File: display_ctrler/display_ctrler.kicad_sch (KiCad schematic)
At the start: 48 parts, among them J101 CONN_01x02, J301 USB_C_Receptacle_USB2.0, J302 Micro_SD_Card, U301 USBLC6-2SC6, U302 W25Q128JVS, U303 RP2040, U304 74AHC04, U305 ESP01s, Y301 12MHz

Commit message: finish schm
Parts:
- C301, C302, C304, C305, C306, C307, C308, C309, C310, C311, C312, C313, C314, C315, C316, C318: footprint Capacitor_SMD:C_0402_1005Metric -> Capacitor_SMD:C_0603_1608Metric
- J301: footprint my_footprints:USB_C_7082A -> project_lib:CUI_UJ20-C-V-C-1-SMT-TR
- R301, R302, R303, R304, R305, R306, R307, R308, R309, R311, R312, R313: footprint Resistor_SMD:R_0402_1005Metric -> Resistor_SMD:R_0603_1608Metric
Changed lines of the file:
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@@
 			)
 		)
-		(property "Footprint" "my_footprints:USB_C_7082A"
+		(property "Footprint" "project_lib:CUI_UJ20-C-V-C-1-SMT-TR"
 			(at 33.02 53.34 0)
 			(effects
@@
 			)
 		)
-		(property "Datasheet" "https://www.usb.org/sites/default/files/documents/usb_type-c.zip"
+		(property "Datasheet" "https://www.sameskydevices.com/product/resource/uj20-c-v-c-1-smt-tr.pdf"
 			(at 33.02 53.34 0)
 			(effects
@@
 			)
 		)
-		(property "Footprint" "Resistor_SMD:R_0402_1005Metric"
+		(property "Footprint" "Resistor_SMD:R_0603_1608Metric"
 			(at 276.098 72.39 90)
 			(effects
@@
 			)
 		)
-		(property "Footprint" "Resistor_SMD:R_0402_1005Metric"
+		(property "Footprint" "Resistor_SMD:R_0603_1608Metric"
 			(at 57.15 104.648 90)
 			(effects
@@
 			)
 		)
-		(property "Footprint" "Resistor_SMD:R_0402_1005Metric"
+		(property "Footprint" "Resistor_SMD:R_0603_1608Metric"
 			(at 265.938 72.39 90)
 			(effects
@@
 			)
 		)
-		(property "Footprint" "Resistor_SMD:R_0402_1005Metric"
+		(property "Footprint" "Resistor_SMD:R_0603_1608Metric"
 			(at 41.91 104.648 90)
 			(effects
@@
 			)
 		)
-		(property "Footprint" "Resistor_SMD:R_0402_1005Metric"
+		(property "Footprint" "Resistor_SMD:R_0603_1608Metric"
 			(at 235.458 71.12 90)
 			(effects
@@
 			)
 		)
-		(property "Footprint" "Resistor_SMD:R_0402_1005Metric"
+		(property "Footprint" "Resistor_SMD:R_0603_1608Metric"
 			(at 48.26 47.498 90)
 			(effects
@@
 			)
 		)
-		(property "Footprint" "Capacitor_SMD:C_0402_1005Metric"
+		(property "Footprint" "Capacitor_SMD:C_0603_1608Metric"
 			(at 120.3452 134.62 0)
 			(effects
@@
 			)
 		)
-		(property "Footprint" "Resistor_SMD:R_0402_1005Metric"
+		(property "Footprint" "Resistor_SMD:R_0603_1608Metric"
 			(at 131.318 64.77 90)
 			(effects
@@
 			)
 		)
-		(property "Footprint" "Capacitor_SMD:C_0402_1005Metric"
+		(property "Footprint" "Capacitor_SMD:C_0603_1608Metric"
 			(at 230.1748 36.83 0)
 			(effects
@@
 			)
 		)
-		(property "Footprint" "Capacitor_SMD:C_0402_1005Metric"
+		(property "Footprint" "Capacitor_SMD:C_0603_1608Metric"
 			(at 218.7448 36.83 0)
 			(effects
@@
 			)
 		)
-		(property "Footprint" "Resistor_SMD:R_0402_1005Metric"
+		(property "Footprint" "Resistor_SMD:R_0603_1608Metric"
 			(at 121.92 80.518 90)
 			(effects
@@
 			)
 		)
-		(property "Footprint" "Capacitor_SMD:C_0402_1005Metric"
+		(property "Footprint" "Capacitor_SMD:C_0603_1608Metric"
 			(at 180.6448 49.53 0)
 			(effects
@@
 			)
 		)
-		(property "Footprint" "Capacitor_SMD:C_0402_1005Metric"
+		(property "Footprint" "Capacitor_SMD:C_0603_1608Metric"
 			(at 68.8848 93.98 0)
 			(effects
@@
 			)
 		)
-		(property "Footprint" "Capacitor_SMD:C_0402_1005Metric"
+		(property "Footprint" "Capacitor_SMD:C_0603_1608Metric"
 			(at 120.3452 116.84 0)
 			(effects
@@
 			)
 		)
-		(property "Footprint" "Capacitor_SMD:C_0402_1005Metric"
+		(property "Footprint" "Capacitor_SMD:C_0603_1608Metric"
 			(at 138.7348 36.83 0)
 			(effects
@@
 			)
 		)
-		(property "Footprint" "Capacitor_SMD:C_0402_1005Metric"
+		(property "Footprint" "Capacitor_SMD:C_0603_1608Metric"
 			(at 241.6048 36.83 0)
 			(effects
@@
 			)
 		)
-		(property "Footprint" "Resistor_SMD:R_0402_1005Metric"
+		(property "Footprint" "Resistor_SMD:R_0603_1608Metric"
 			(at 121.92 83.058 90)
 			(effects
@@
 			)
 		)
-		(property "Footprint" "Capacitor_SMD:C_0402_1005Metric"
+		(property "Footprint" "Capacitor_SMD:C_0603_1608Metric"
 			(at 173.0248 36.83 0)
 			(effects
@@
 			)
 		)
-		(property "Footprint" "Capacitor_SMD:C_0402_1005Metric"
+		(property "Footprint" "Capacitor_SMD:C_0603_1608Metric"
 			(at 150.1648 36.83 0)
 			(effects
@@
 			)
 		)
-		(property "Footprint" "Capacitor_SMD:C_0402_1005Metric"
+		(property "Footprint" "Capacitor_SMD:C_0603_1608Metric"
 			(at 207.3148 36.83 0)
 			(effects
@@
 			)
 		)
-		(property "Footprint" "Resistor_SMD:R_0402_1005Metric"
+		(property "Footprint" "Resistor_SMD:R_0603_1608Metric"
 			(at 220.218 71.12 90)
 			(effects
@@
 			)
 		)
-		(property "Footprint" "Capacitor_SMD:C_0402_1005Metric"
+		(property "Footprint" "Capacitor_SMD:C_0603_1608Metric"
 			(at 91.7448 151.13 0)
 			(effects
@@
 			)
 		)
-		(property "Footprint" "Capacitor_SMD:C_0402_1005Metric"
+		(property "Footprint" "Capacitor_SMD:C_0603_1608Metric"
 			(at 65.0748 38.1 0)
 			(effects
@@
 			)
 		)
-		(property "Footprint" "Capacitor_SMD:C_0402_1005Metric"
+		(property "Footprint" "Capacitor_SMD:C_0603_1608Metric"
 			(at 195.8848 36.83 0)
 			(effects
@@
 			)
 		)
-		(property "Footprint" "Capacitor_SMD:C_0402_1005Metric"
+		(property "Footprint" "Capacitor_SMD:C_0603_1608Metric"
 			(at 184.4548 36.83 0)
 			(effects
@@
 			)
 		)
-		(property "Footprint" "Resistor_SMD:R_0402_1005Metric"
+		(property "Footprint" "Resistor_SMD:R_0603_1608Metric"
 			(at 48.26 44.958 90)
 			(effects
@@
 			)
 		)
-		(property "Footprint" "Resistor_SMD:R_0402_1005Metric"
+		(property "Footprint" "Resistor_SMD:R_0603_1608Metric"
 			(at 129.54 128.778 90)
 			(effects
@@
 			)
 		)
-		(property "Footprint" "Capacitor_SMD:C_0402_1005Metric"
+		(property "Footprint" "Capacitor_SMD:C_0603_1608Metric"
 			(at 150.1648 49.53 0)
 			(effects

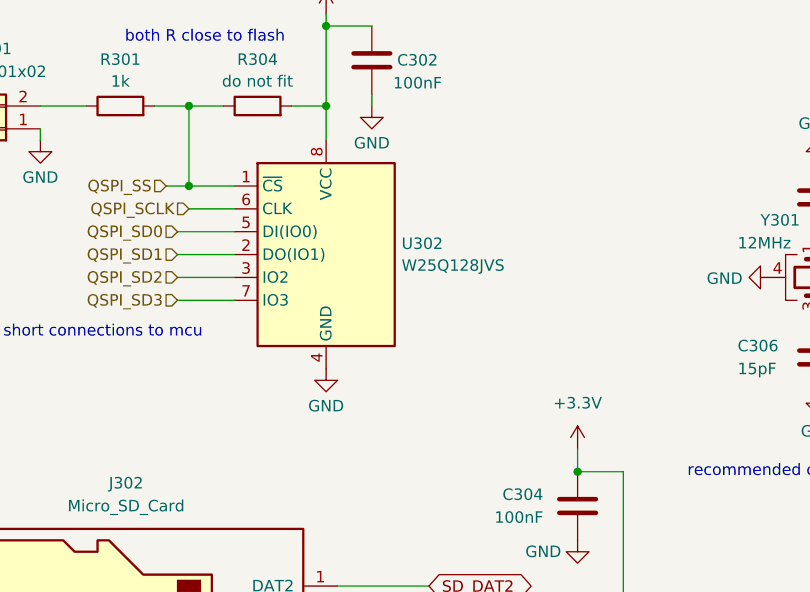
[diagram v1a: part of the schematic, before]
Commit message: start power rx
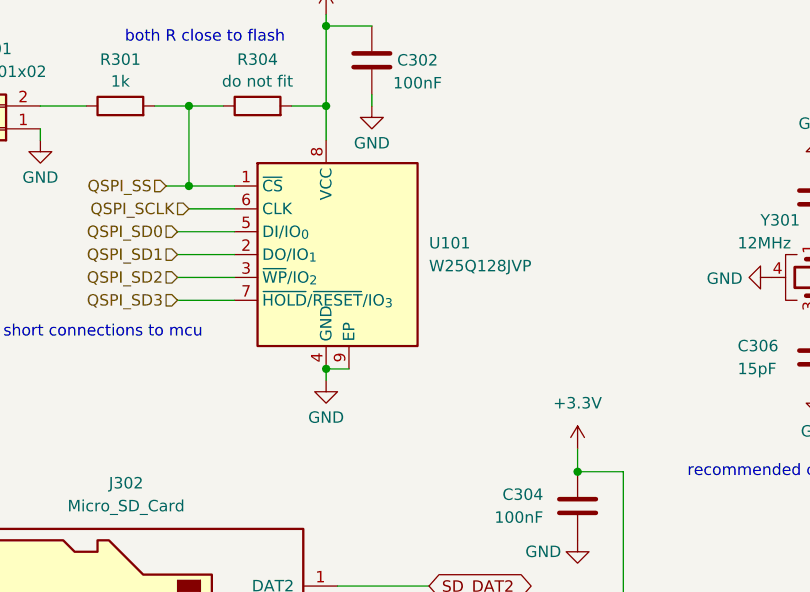
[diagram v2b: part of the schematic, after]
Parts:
- removed U302: W25Q128JVS, Package_SO:SOIC-8_5.3x5.3mm_P1.27mm, symbol Memory_Flash:W25Q128JVS
- added U101: W25Q128JVP, Package_SON:WSON-8-1EP_6x5mm_P1.27mm_EP3.4x4.3mm, symbol Memory_Flash:W25Q128JVP
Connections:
- net +3.3V: now also U101.8 (VCC)
- net GND: now also U101.4 (GND), U101.9 (EP)
- net QSPI_SCLK: now also U101.6 (CLK)
- net QSPI_SD0: now also U101.5 (DI/IO_{0})
- net QSPI_SD1: now also U101.2 (DO/IO_{1})
- net QSPI_SD2: now also U101.3 (~{WP}/IO_{2})
- net QSPI_SD3: now also U101.7 (~{HOLD}/~{RESET}/IO_{3})
- net QSPI_SS: now also U101.1 (~{CS})
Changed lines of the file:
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@@
 	)
 	(junction
+		(at 64.77 132.08)
+		(diameter 0)
+		(color 0 0 0 0)
+	)
+	(junction
 		(at 160.02 49.53)
 		(diameter 0)
@@
 	(wire
 		(pts
+			(xy 64.77 133.35) (xy 64.77 132.08)
+		)
+		(stroke
+			(width 0)
+			(type default)
+		)
+	)
+	(wire
+		(pts
 			(xy 64.77 102.87) (xy 60.96 102.87)
 		)
@@
 	(wire
 		(pts
+			(xy 64.77 132.08) (xy 67.31 132.08)
+		)
+		(stroke
+			(width 0)
+			(type default)
+		)
+	)
+	(wire
+		(pts
 			(xy 160.02 59.69) (xy 160.02 63.5)
 		)
@@
 	)
 	(symbol
+		(lib_id "Memory_Flash:W25Q128JVP")
+		(at 64.77 119.38 0)
+		(unit 1)
+		(exclude_from_sim no)
+		(in_bom yes)
+		(on_board yes)
+		(dnp no)
+		(fields_autoplaced yes)
+		(property "Reference" "U101"
+			(at 76.2 118.1099 0)
+			(effects
+				(font
+					(size 1.27 1.27)
+				)
+				(justify left)
+			)
+		)
+		(property "Value" "W25Q128JVP"
+			(at 76.2 120.6499 0)
+			(effects
+				(font
+					(size 1.27 1.27)
+				)
+				(justify left)
+			)
+		)
+		(property "Footprint" "Package_SON:WSON-8-1EP_6x5mm_P1.27mm_EP3.4x4.3mm"
+			(at 64.77 96.52 0)
+			(effects
+				(font
+					(size 1.27 1.27)
+				)
+				(hide yes)
+			)
+		)
+		(property "Datasheet" "https://www.winbond.com/resource-files/w25q128jv_dtr%20revc%2003272018%20plus.pdf"
+			(at 64.77 93.98 0)
+			(effects
+				(font
+					(size 1.27 1.27)
+				)
+				(hide yes)
+			)
+		)
+		(property "Description" "128Mbit / 16MiB Serial Flash Memory, Standard/Dual/Quad SPI, 2.7-3.6V, WSON-8"
+			(at 64.77 91.44 0)
+			(effects
+				(font
+					(size 1.27 1.27)
+				)
+				(hide yes)
+			)
+		)
+		(pin "5"
+		)
+		(pin "2"
+		)
+		(pin "9"
+		)
+		(pin "4"
+		)
+		(pin "8"
+		)
+		(pin "3"
+		)
+		(pin "7"
+		)
+		(pin "1"
+		)
+		(pin "6"
+		)
+		(instances
+			(project ""
+				(path "/9292a425-4deb-48f6-8b98-43cd7d592040"
+					(reference "U101")
+					(unit 1)
+				)
+			)
+		)
+	)
+	(symbol
 		(lib_id "power:+3.3V")
 		(at 64.77 92.71 0)
@@
 	(symbol
 		(lib_id "power:GND")
-		(at 64.77 132.08 0)
+		(at 64.77 133.35 0)
 		(unit 1)
 		(exclude_from_sim no)
@@
 		(fields_autoplaced yes)
 		(property "Reference" "#PWR0308"
-			(at 64.77 138.43 0)
+			(at 64.77 139.7 0)
 			(effects
 				(font
@@
 		)
 		(property "Value" "GND"
-			(at 64.77 136.2131 0)
+			(at 64.77 137.4831 0)
 			(effects
 				(font
@@
 		)
 		(property "Footprint" ""
-			(at 64.77 132.08 0)
+			(at 64.77 133.35 0)
 			(effects
 				(font
@@
 		)
 		(property "Datasheet" ""
-			(at 64.77 132.08 0)
+			(at 64.77 133.35 0)
 			(effects
 				(font
@@
 		)
 		(property "Description" ""
-			(at 64.77 132.08 0)
+			(at 64.77 133.35 0)
 			(effects
 				(font
@@
 					(unit 1)
 				)
-			)
-		)
-	)
-	(symbol
-		(lib_id "Memory_Flash:W25Q128JVS")
-		(at 64.77 119.38 0)
-		(unit 1)
-		(exclude_from_sim no)
-		(in_bom yes)
-		(on_board yes)
-		(dnp no)
-		(fields_autoplaced yes)
-		(property "Reference" "U302"
-			(at 73.152 118.1679 0)
-			(effects
-				(font
-					(size 1.27 1.27)
-				)
-				(justify left)
-			)
-		)
-		(property "Value" "W25Q128JVS"
-			(at 73.152 120.5921 0)
-			(effects
-				(font
-					(size 1.27 1.27)
-				)
-				(justify left)
-			)
-		)
-		(property "Footprint" "Package_SO:SOIC-8_5.3x5.3mm_P1.27mm"
-			(at 64.77 119.38 0)
-			(effects
-				(font
-					(size 1.27 1.27)
-				)
-				(hide yes)
-			)
-		)
-		(property "Datasheet" "https://mm.digikey.com/Volume0/opasdata/d220001/medias/docus/7161/256_W25Q128JV.pdf"
-			(at 64.77 119.38 0)
-			(effects
-				(font
-					(size 1.27 1.27)
-				)
-				(hide yes)
-			)
-		)
-		(property "Description" ""
-			(at 64.77 119.38 0)
-			(effects
-				(font
-					(size 1.27 1.27)
-				)
-				(hide yes)
-			)
-		)
-		(property "LCSC" "C97521"
-			(at 64.77 119.38 0)
-			(effects
-				(font
-					(size 1.27 1.27)
-				)
-				(hide yes)
-			)
-		)
-		(pin "1"
-		)
-		(pin "2"
-		)
-		(pin "3"
-		)
-		(pin "4"
-		)
-		(pin "5"
-		)
-		(pin "6"
-		)
-		(pin "7"
-		)
-		(pin "8"
-		)
-		(instances
-			(project "display_ctrler"
-				(path "/9292a425-4deb-48f6-8b98-43cd7d592040"
-					(reference "U302")
-					(unit 1)
-				)

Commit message: start disp pcb layout
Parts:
- removed U201: ~, my_footprints:slot, symbol my_symbols:pin
- removed U202, U203: ~, my_footprints:edge_contact, symbol my_symbols:slot1
- removed U204, U205, U206, U207: ~, my_footprints:edge_contact_small, symbol my_symbols:slot1
- removed U208, U209, U210: ~, my_footprints:JLC_tooling_hole, symbol my_symbols:JLCPCB
- removed U304: 74AHC04, Package_SO:SOIC-14_3.9x8.7mm_P1.27mm, symbol 74xx:74AHCT04
- added U1: SN74AHC1G14DBVR, Package_TO_SOT_SMD:SOT-23-5, symbol symbols:SN74AHC1G14DBVR
- C307, C308, C309, C318: footprint Capacitor_SMD:C_0603_1608Metric -> Capacitor_SMD:C_0402_1005Metric
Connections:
- net +3.3V: now also U1.5
- net GND: now also J301.SH1, J301.SH2, J301.SH3, J301.SH4, J302.G1, J302.G2, J302.G3, J302.G4, U1.3; no longer J302.10 (S), J302.11 (S), J302.12 (S), J302.13 (S)
- net Hall: now also U1.2
- net _Hall_: now also U1.4
- no-connect marks 26 -> 27
